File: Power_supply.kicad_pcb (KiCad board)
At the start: 2 copper layers, 160 x 40 mm, 51 parts, among them J1 Transformers, J20 HV_Transformer, J21 LV_Transformer, J22 220V, J23 Transformers, J24 Thyratrone, J25 Anodes_enable, J26 Conn_01x04, J27 Conn_01x04, J28 Conn_01x04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

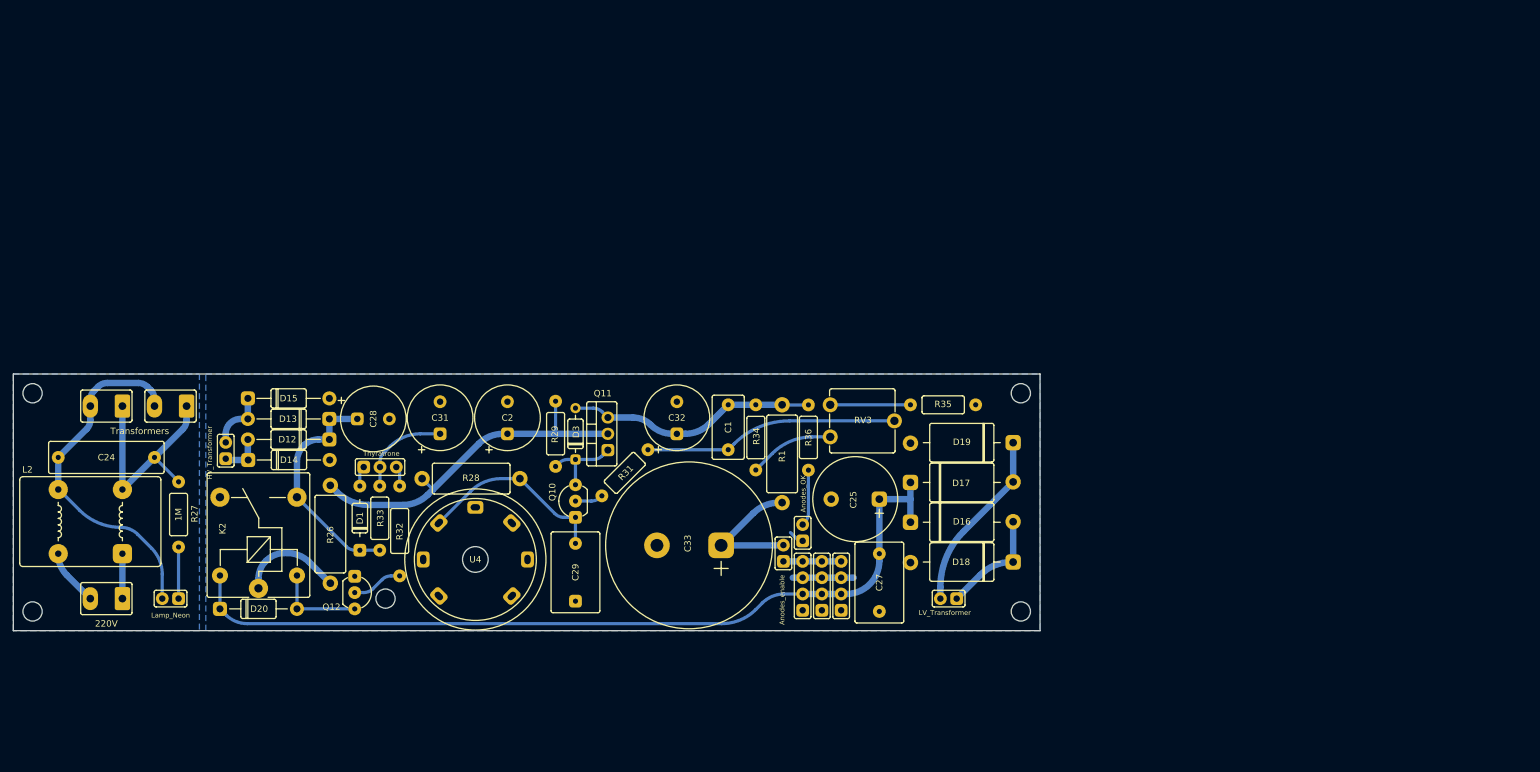
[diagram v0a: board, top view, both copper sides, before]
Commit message: Started redesigning power supply
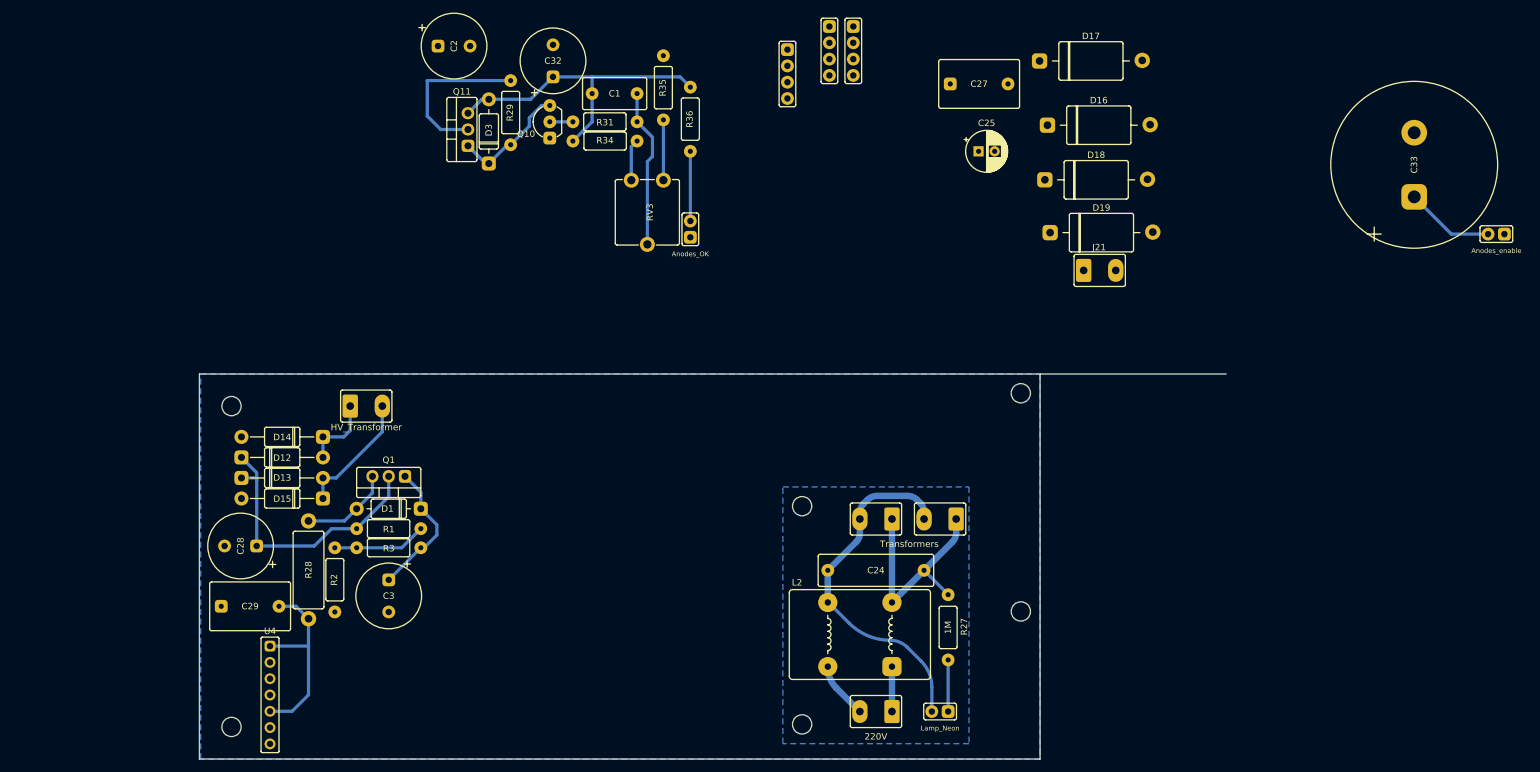
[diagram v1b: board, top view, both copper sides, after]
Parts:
- removed C31: 10uF, spdf1626_lib:C_THT_D10.0mm_P5.00mm
- removed D20: 1n4007, spdf1626_lib:D_DO-41
- removed J24: Thyratrone, spdf1626_lib:PinHeader_1x03_P2.54mm
- removed K2: SANYOU_SRD_Form_C, spdf1626_lib:Relay_THT_SRD_Series
- removed Q12: 2N3904, spdf1626_lib:TO-92_Wide
- removed R26: 100R, spdf1626_lib:R_THT_1W
- removed R32: 100k, spdf1626_lib:R_THT_025W
- removed R33: 1M, spdf1626_lib:R_THT_025W
- added C3: 2,2uF, spdf1626_lib:C_THT_D10.0mm_P5.00mm, F.Cu at (88.5, 124.6)
- added Q1: STP4NK60ZFP(MJE13003), spdf1626_lib:TO-220-3_Vertical, F.Cu at (88.5, 106.0)
- added R2: 10M, spdf1626_lib:R_THT_025W, F.Cu at (80.1, 122.1)
- added R3: 100, spdf1626_lib:R_THT_025W, F.Cu at (88.5, 117.1)
- C25: footprint spdf1626_lib:C_THT_D13.0mm_P7.50mm -> Capacitor_THT:CP_Radial_D6.3mm_P2.50mm
- C33: footprint spdf1626_lib:C_THT_D22.0mm_P10.00mm -> Capacitor_THT:CP_Radial_D22.0mm_P10.00mm_SnapIn
- D1: value BZX55C75 -> 1N4740A; footprint spdf1626_lib:D_THT_DO-35_SOD27_Horizontal -> spdf1626_lib:D_DO-41_short
- D3: footprint spdf1626_lib:D_THT_DO-35_SOD27_Horizontal -> spdf1626_lib:D_DO-41_short
- J20, J21: footprint spdf1626_lib:PinHeader_1x02_P2.54mm -> spdf1626_lib:Connector_1x02_P5mm_Vertical
- R1: value 100R -> 330k; footprint spdf1626_lib:R_THT_1W -> spdf1626_lib:R_THT_025W
- U4: footprint spdf1626_lib:7-pin_tube_socket -> spdf1626_lib:PinHeader_1x07_P2.54mm
- moved C33 127.6 mm to (248.3, 57.4), turned to 90 degrees
- moved J25 123.4 mm to (262.3, 68.2), turned to -90 degrees
- moved C24 121.2 mm to (164.4, 120.6)
- moved J1 121.2 mm to (164.4, 112.6)
- moved J22 121.2 mm to (164.4, 142.6)
- moved J23 121.2 mm to (174.4, 112.6)
- moved L2 121.2 mm to (161.9, 130.6)
- moved NE3 121.2 mm to (175.7, 142.6)
- moved R27 121.2 mm to (175.7, 124.4)
- moved J27 91.1 mm to (160.9, 35.9), turned to 0 degrees
- moved J26 91.0 mm to (157.2, 35.9), turned to 0 degrees
- moved J28 87.4 mm to (150.6, 39.5), turned to 0 degrees
- moved C27 79.2 mm to (180.5, 44.8), turned to 0 degrees
- moved D17 68.7 mm to (197.9, 41.2)
- moved D16 65.5 mm to (199.2, 51.2)
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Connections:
- C2 pad 1: Net-(C2-Pad1) -> Net-(Q11-Pad2)
- C33 pad 1: Net-(C33-Pad1) -> Net-(C1-Pad2)
- D1 pad 1: HV -> Net-(C3-Pad1)
- D1 pad 2: Net-(D1-Pad2) -> Net-(Q11-Pad2)
- J25 pad 2: Net-(C33-Pad1) -> Net-(C1-Pad2)
- Q11 pad 2: Net-(C2-Pad1) -> Net-(Q11-Pad2)
- R1 pad 1: Net-(C1-Pad2) -> Net-(R1-Pad1)
- R1 pad 2: Net-(C33-Pad1) -> HV
- R28 pad 1: Net-(C2-Pad1) -> Net-(Q11-Pad2)
- R29 pad 2: Net-(C2-Pad1) -> Net-(Q11-Pad2)
- U4 pad 1: unconnected-(U4-Pad1) -> Net-(C29-Pad2)
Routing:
- net +6V: track 134.0 -> 0.00 mm
- net Net-(C2-Pad1): track 55.7 -> 0.00 mm
- net Net-(Q11-Pad2): track 0.00 -> 40.1 mm
- net Net-(D17-Pad2): track 28.4 -> 0.00 mm
- net Net-(C1-Pad2): track 39.1 -> 62.8 mm
- net Net-(C33-Pad1): track 21.7 -> 0.00 mm
- net Net-(C3-Pad1): track 0.00 -> 21.6 mm
- net Net-(D16-Pad2): track 17.1 -> 0.00 mm
- net K1.1: track 16.6 -> 0.00 mm
- net Net-(C31-Pad1): track 15.0 -> 0.00 mm
- net Net-(C1-Pad1): track 39.7 -> 24.8 mm
- net Net-(R1-Pad1): track 0.00 -> 14.6 mm
- net Net-(D20-Pad2): track 14.2 -> 0.00 mm
- net GND: track 11.9 -> 0.00 mm
- net Net-(D13-Pad2): track 9.23 -> 19.4 mm
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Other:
- board size 160 x 40 mm -> 160 x 60 mm

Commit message: Continue rebuilding power supply PCB
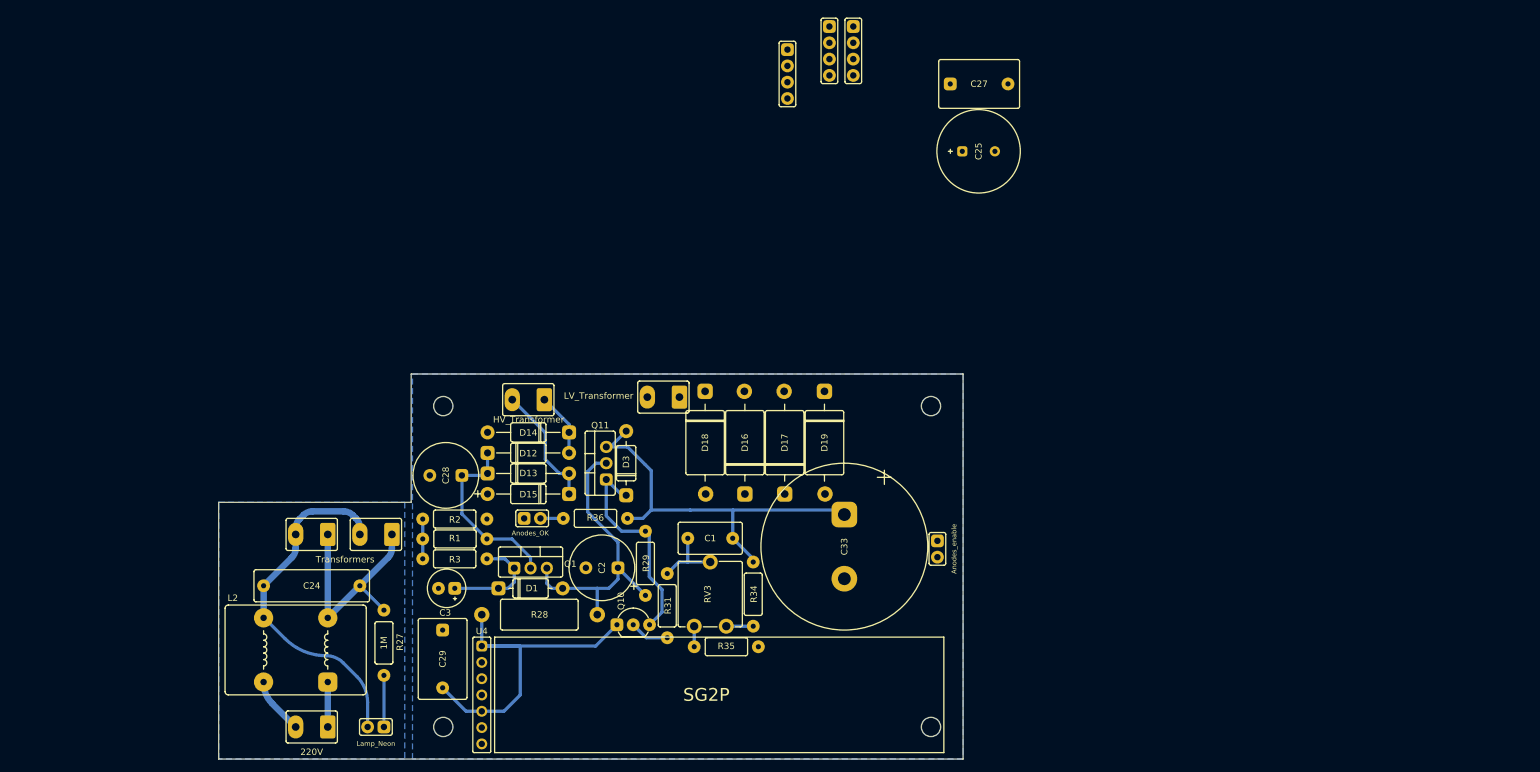
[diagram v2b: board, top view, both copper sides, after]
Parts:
- removed C32: 10uF, spdf1626_lib:C_THT_D10.0mm_P5.00mm
- C25: footprint Capacitor_THT:CP_Radial_D6.3mm_P2.50mm -> spdf1626_lib:C_THT_D13mm_P5.08mm
- C3: footprint spdf1626_lib:C_THT_D10.0mm_P5.00mm -> spdf1626_lib:C_THT_D5.0mm_P2.54mm
- moved C33 106.9 mm to (159.5, 116.9), turned to -90 degrees
- moved J25 100.5 mm to (174.0, 116.0), turned to 0 degrees
- moved C24 88.0 mm to (76.5, 123.0)
- moved J1 88.0 mm to (76.5, 115.0)
- moved J22 88.0 mm to (76.5, 145.0)
- moved J23 88.0 mm to (86.5, 115.0)
- moved L2 88.0 mm to (74.0, 133.0)
- moved NE3 88.0 mm to (87.8, 145.0)
- moved R27 88.0 mm to (87.8, 126.8)
- moved R35 87.6 mm to (141.1, 132.5), turned to 0 degrees
- moved C2 84.5 mm to (121.7, 120.2), turned to 180 degrees
- moved Q10 79.4 mm to (126.6, 129.1), turned to 0 degrees
- moved D17 76.3 mm to (150.2, 100.7), turned to 90 degrees
- moved R31 76.0 mm to (131.9, 126.1), turned to -90 degrees
- moved R34 74.3 mm to (145.3, 124.3), turned to -90 degrees
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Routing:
- net Net-(C29-Pad2): track 30.3 -> 55.6 mm
- net Net-(D3-Pad1): track 18.4 -> 35.4 mm
- net HV: track 44.4 -> 28.5 mm
- net Net-(C1-Pad1): track 24.8 -> 11.1 mm
- net Net-(R1-Pad1): track 14.6 -> 6.20 mm
- net Net-(NE4-Pad2): track 10.9 -> 3.56 mm
- net Net-(Q11-Pad2): track 40.1 -> 46.7 mm
- net Net-(R35-Pad1): track 9.40 -> 3.20 mm
- net Net-(C3-Pad1): track 21.6 -> 16.7 mm
- net Net-(R31-Pad2): track 3.60 -> 6.14 mm
- net Net-(R34-Pad2): track 6.47 -> 4.20 mm
- net Net-(D12-Pad2): track 11.7 -> 9.89 mm
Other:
- board size 160 x 60 mm -> 116 x 60 mm
- board text added: "SG2P"

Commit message: PCB almost done
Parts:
- removed C27: 100n, spdf1626_lib:C_THT_K73-17_P9.00mm
- removed J26, J27, J28: Conn_01x04, spdf1626_lib:PinHeader_1x04_P2.54mm
- added J2: 240V, spdf1626_lib:Connector_1x02_P5mm_Vertical, F.Cu at (173.4, 103.5)
- added J3: 6V3, spdf1626_lib:Connector_1x02_P5mm_Vertical, F.Cu at (167.8, 95.2)
- moved C25 47.2 mm to (158.5, 97.1), turned to 90 degrees
- moved NE4 37.2 mm to (146.7, 114.3), turned to -90 degrees
- moved R36 19.4 mm to (139.2, 118.3), turned to 180 degrees
- moved R34 15.1 mm to (131.0, 119.3)
- moved J21 10.8 mm to (120.5, 94.0)
- moved R35 10.7 mm to (147.4, 123.8), turned to -90 degrees
- moved J25 9.92 mm to (173.4, 125.9)
- moved R31 8.27 mm to (127.2, 119.3)
- moved RV3 7.56 mm to (144.2, 122.4), turned to 180 degrees
- moved D16 7.50 mm to (136.5, 100.7)
- moved D17 7.50 mm to (142.7, 100.7)
- moved D18 7.50 mm to (130.3, 100.7)
- moved D19 7.50 mm to (148.9, 100.7)
- moved Q1 5.79 mm to (107.5, 115.4), turned to 90 degrees
- moved D1 5.58 mm to (110.6, 117.8), turned to 90 degrees
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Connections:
- RV3 pad 1: Net-(R34-Pad2) -> Net-(R35-Pad1)
- RV3 pad 3: Net-(R35-Pad1) -> Net-(R34-Pad2)
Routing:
- net +6V: track 0.00 -> 37.1 mm
- net Net-(D17-Pad2): track 0.00 -> 34.3 mm
- net 240V: track 0.00 -> 19.9 mm
- net Net-(C1-Pad2): track 62.8 -> 80.2 mm
- net Net-(D16-Pad2): track 0.00 -> 14.0 mm
- net Net-(C1-Pad1): track 11.1 -> 23.4 mm
- net Net-(D3-Pad1): track 35.4 -> 23.4 mm
- net Net-(R34-Pad2): track 4.20 -> 15.1 mm
- net Net-(C29-Pad2): track 55.6 -> 49.9 mm
- net HV: track 28.5 -> 23.5 mm
- net GND: track 0.00 -> 3.21 mm
- net Net-(C2-Pad1): track 46.7 -> 44.0 mm
- net Net-(Q10-Pad2): track 6.14 -> 3.90 mm
- net Net-(R35-Pad1): track 3.20 -> 4.93 mm
- net Net-(R1-Pad1): track 6.20 -> 5.30 mm

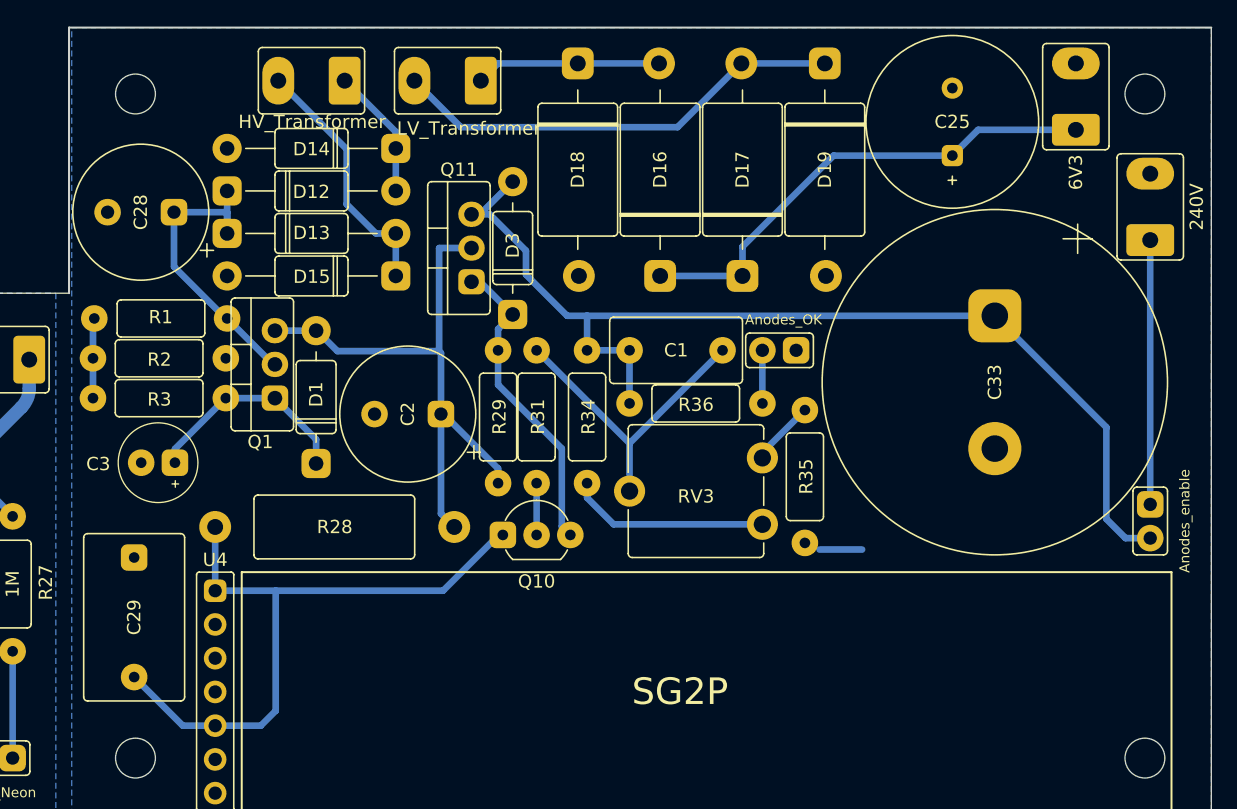
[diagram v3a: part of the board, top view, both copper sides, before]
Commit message: Rounded traces
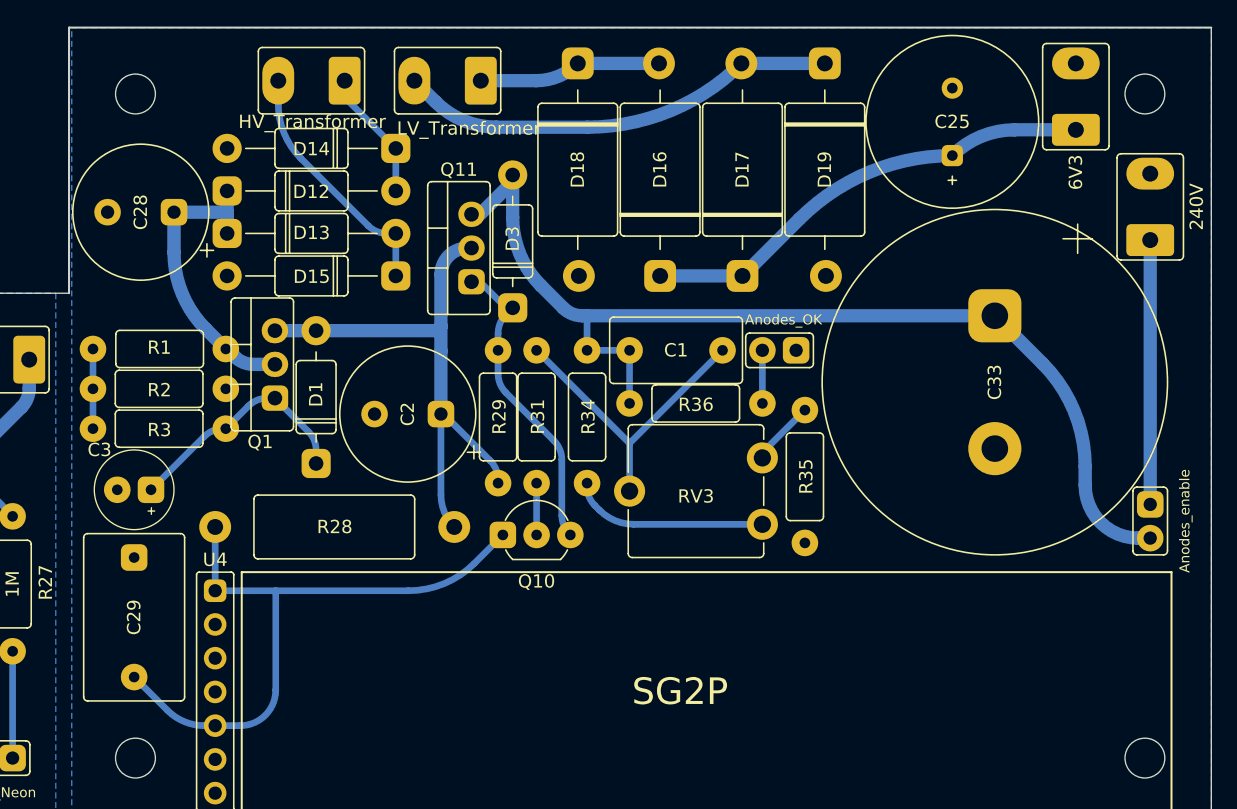
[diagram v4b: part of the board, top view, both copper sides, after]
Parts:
- moved C3 2.72 mm to (96.9, 124.8)
- moved R1 2.30 mm to (98.8, 114.2)
- moved R2 2.30 mm to (98.8, 117.2)
- moved R3 2.30 mm to (98.8, 120.2)
- moved D3 0.50 mm to (125.4, 106.1)
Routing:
- net GND: track 3.21 -> 0.00 mm
- net +6V: track 37.1 -> 34.8 mm
- net Net-(C2-Pad1): track 44.0 -> 42.2 mm
- net Net-(C3-Pad1): track 16.4 -> 18.1 mm
- net Net-(C29-Pad2): track 49.9 -> 48.8 mm
- net Net-(D17-Pad2): track 34.3 -> 33.2 mm
- net HV: track 23.5 -> 24.5 mm
- net Net-(R1-Pad1): track 5.30 -> 6.04 mm
